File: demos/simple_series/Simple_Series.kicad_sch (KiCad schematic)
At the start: 3 parts, among them SW1 SPST

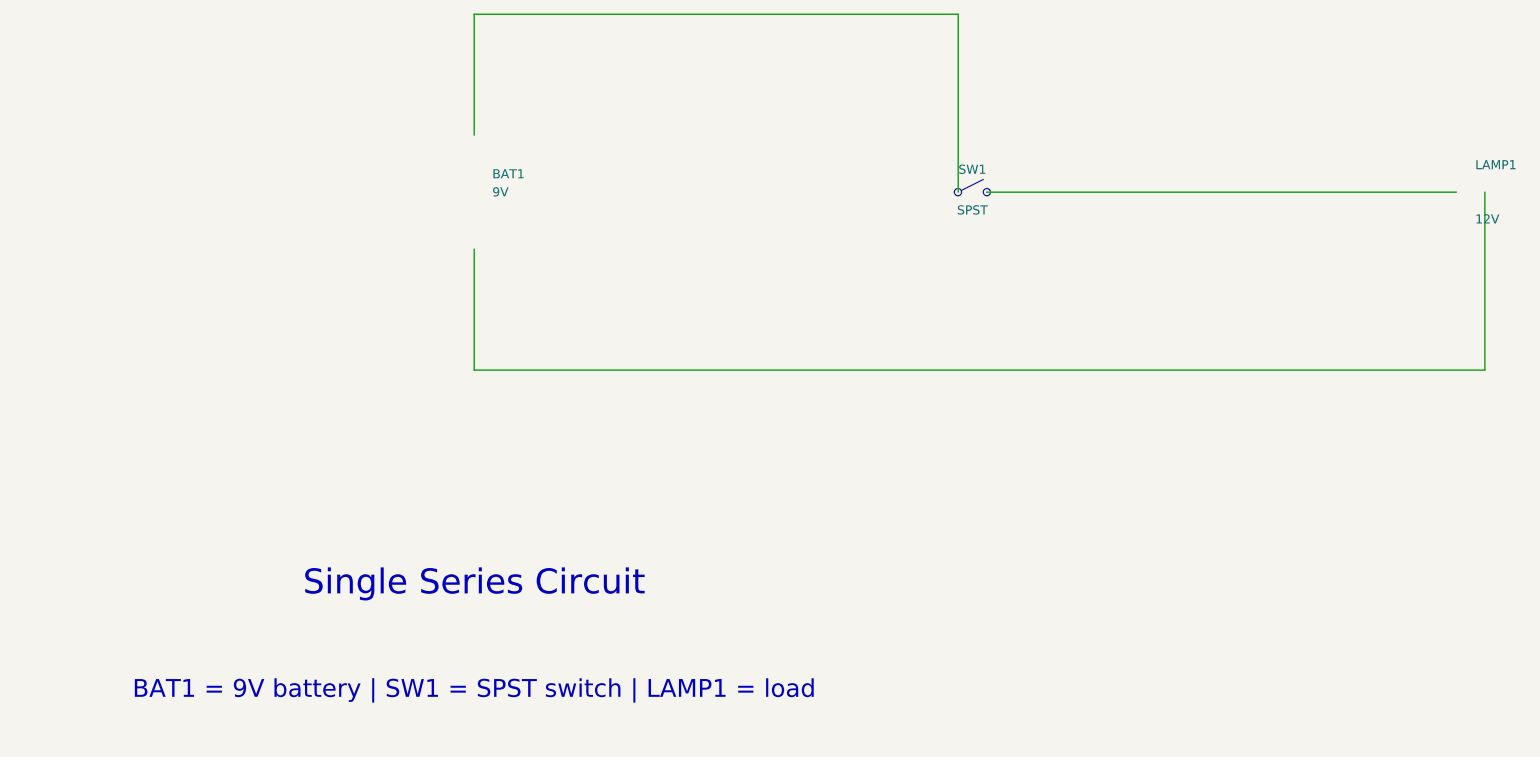
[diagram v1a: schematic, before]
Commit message: feat: pin-aware schematic drawing (connect wires to exact pins)
- kicad_mcp/symbols.py: parse .kicad_sym pin definitions + rotation
  transform (0/90/180/270, matches SCH_SYMBOL transform)
- kicad_sch_add_symbol now returns each pin's absolute coordinate (incl.
  rotation); new kicad_sch_get_symbol_pins and kicad_sch_connect tools
  (connect by pin name, auto-routed Z-shape with optional via point)
- fix float truncation bug: int(x*MM) lost 1 IU (e.g. 134.9199 vs 1349200)
  so wires never joined pins (netlist showed all unconnected); use round()

Verified: redrew single-series circuit with LAMP1 rotated 90; wire endpoints
exactly on pins (134.9200 etc); kicad-cli netlist now shows all 6 pins in a
single connected net.
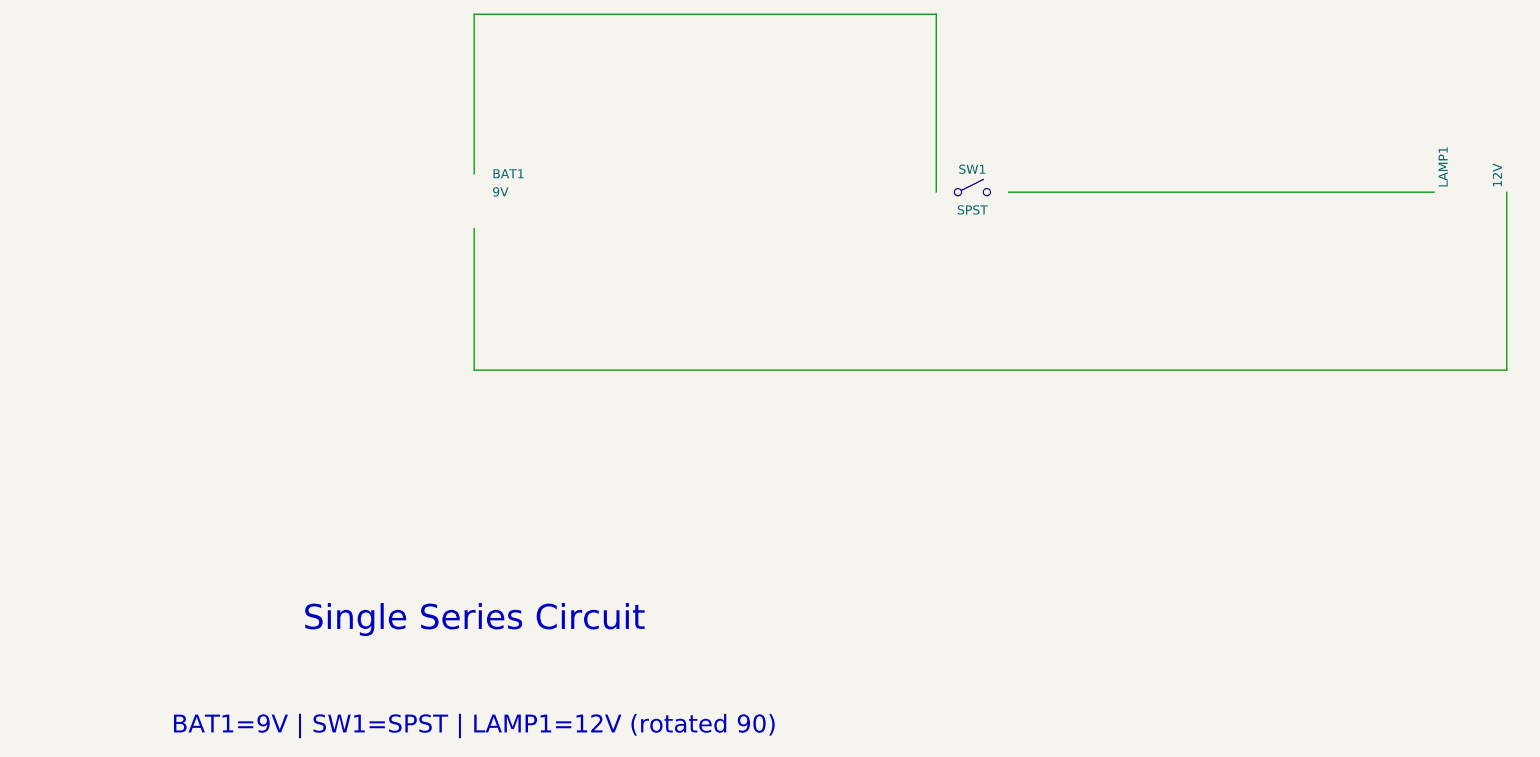
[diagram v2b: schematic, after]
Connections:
- net at SW1.2 (B): now also LAMP1.2 (+)
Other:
- note added: "BAT1=9V | SW1=SPST | LAMP1=12V (rotated 90)"
- note removed: "BAT1 = 9V battery | SW1 = SPST switch | LAMP1 = load"
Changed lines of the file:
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@@
 	(text "Single Series Circuit"
 		(exclude_from_sim no)
-		(at 70 135 0)
+		(at 70 140 0)
 		(effects
 			(font
@@
 		)
 	)
-	(text "BAT1 = 9V battery | SW1 = SPST switch | LAMP1 = load"
-		(exclude_from_sim no)
-		(at 70 150 0)
+	(text "BAT1=9V | SW1=SPST | LAMP1=12V (rotated 90)"
+		(exclude_from_sim no)
+		(at 70 155 0)
 		(effects
 			(font
@@
 	(wire
 		(pts
-			(xy 212 80) (xy 212 105)
-		)
-		(stroke
-			(width 0)
-			(type default)
-		)
-	)
-	(wire
-		(pts
-			(xy 142 80) (xy 208 80)
-		)
-		(stroke
-			(width 0)
-			(type default)
-		)
-	)
-	(wire
-		(pts
-			(xy 70 72) (xy 70 55)
-		)
-		(stroke
-			(width 0)
-			(type default)
-		)
-	)
-	(wire
-		(pts
-			(xy 70 105) (xy 70 88)
-		)
-		(stroke
-			(width 0)
-			(type default)
-		)
-	)
-	(wire
-		(pts
-			(xy 70 55) (xy 138 55)
-		)
-		(stroke
-			(width 0)
-			(type default)
-		)
-	)
-	(wire
-		(pts
-			(xy 138 55) (xy 138 80)
-		)
-		(stroke
-			(width 0)
-			(type default)
-		)
-	)
-	(wire
-		(pts
-			(xy 212 105) (xy 70 105)
-		)
-		(stroke
-			(width 0)
-			(type default)
+			(xy 215.08 80) (xy 215.08 105)
+		)
+		(stroke
+			(width 0)
+			(type default)
+		)
+	)
+	(wire
+		(pts
+			(xy 215.08 105) (xy 70 105)
+		)
+		(stroke
+			(width 0)
+			(type default)
+		)
+	)
+	(wire
+		(pts
+			(xy 70 77.46) (xy 70 55)
+		)
+		(stroke
+			(width 0)
+			(type default)
+		)
+	)
+	(wire
+		(pts
+			(xy 145.08 80) (xy 204.92 80)
+		)
+		(stroke
+			(width 0)
+			(type default)
+		)
+	)
+	(wire
+		(pts
+			(xy 70 105) (xy 70 85.08)
+		)
+		(stroke
+			(width 0)
+			(type default)
+		)
+	)
+	(wire
+		(pts
+			(xy 134.92 55) (xy 134.92 80)
+		)
+		(stroke
+			(width 0)
+			(type default)
+		)
+	)
+	(wire
+		(pts
+			(xy 70 55) (xy 134.92 55)
+		)
+		(stroke
+			(width 0)
+			(type default)
+		)
+	)
+	(symbol
+		(lib_id "Switch:SW_SPST")
+		(at 140 80 0)
+		(unit 1)
+		(body_style 0)
+		(exclude_from_sim no)
+		(in_bom yes)
+		(on_board yes)
+		(in_pos_files yes)
+		(dnp no)
+		(property "Reference" "SW1"
+			(at 140 76.825 0)
+			(show_name no)
+			(do_not_autoplace no)
+			(effects
+				(font
+					(size 1.27 1.27)
+				)
+			)
+		)
+		(property "Value" "SPST"
+			(at 140 82.54 0)
+			(show_name no)
+			(do_not_autoplace no)
+			(effects
+				(font
+					(size 1.27 1.27)
+				)
+			)
+		)
+		(property "Footprint" ""
+			(at 140 80 0)
+			(hide yes)
+			(show_name no)
+			(do_not_autoplace no)
+			(effects
+				(font
+					(size 1.27 1.27)
+				)
+			)
+		)
+		(property "Datasheet" ""
+			(at 140 80 0)
+			(hide yes)
+			(show_name no)
+			(do_not_autoplace no)
+			(effects
+				(font
+					(size 1.27 1.27)
+				)
+			)
+		)
+		(property "Description" "Single Pole Single Throw (SPST) switch"
+			(at 140 80 0)
+			(hide yes)
+			(show_name no)
+			(do_not_autoplace no)
+			(effects
+				(font
+					(size 1.27 1.27)
+				)
+			)
+		)
+		(pin "2"
+		)
+		(pin "1"
+		)
+		(instances
+			(project "Simple_Series"
+				(path "/89df9635-6746-4aa7-a923-2c4181dcf2e4"
+					(reference "SW1")
+					(unit 1)
+				)
+			)
+		)
+	)
+	(symbol
+		(lib_id "Device:Lamp")
+		(at 210 80 90)
+		(unit 1)
+		(body_style 0)
+		(exclude_from_sim no)
+		(in_bom yes)
+		(on_board yes)
+		(in_pos_files yes)
+		(dnp no)
+		(property "Reference" "LAMP1"
+			(at 206.19 79.365 0)
+			(show_name no)
+			(do_not_autoplace no)
+			(effects
+				(font
+					(size 1.27 1.27)
+				)
+				(justify left)
+			)
+		)
+		(property "Value" "12V"
+			(at 213.81 79.365 0)
+			(show_name no)
+			(do_not_autoplace no)
+			(effects
+				(font
+					(size 1.27 1.27)
+				)
+				(justify left)
+			)
+		)
+		(property "Footprint" ""
+			(at 207.46 80 90)
+			(hide yes)
+			(show_name no)
+			(do_not_autoplace no)
+			(effects
+				(font
+					(size 1.27 1.27)
+				)
+			)
+		)
+		(property "Datasheet" ""
+			(at 207.46 80 90)
+			(hide yes)
+			(show_name no)
+			(do_not_autoplace no)
+			(effects
+				(font
+					(size 1.27 1.27)
+				)
+			)
+		)
+		(property "Description" "Lamp"
+			(at 210 80 0)
+			(hide yes)
+			(show_name no)
+			(do_not_autoplace no)
+			(effects
+				(font
+					(size 1.27 1.27)
+				)
+			)
+		)
+		(pin "2"
+		)
+		(pin "1"
+		)
+		(instances
+			(project "Simple_Series"
+				(path "/89df9635-6746-4aa7-a923-2c4181dcf2e4"
+					(reference "LAMP1")
+					(unit 1)
+				)
+			)
 		)
 	)
@@
 		(instances
 			(project "Simple_Series"
-				(path "/fe51f7a9-8c15-422c-9e72-244da0bfb221"
+				(path "/89df9635-6746-4aa7-a923-2c4181dcf2e4"
 					(reference "BAT1")
 					(unit 1)
 				)
-			)
-		)
-	)
-	(symbol
-		(lib_id "Switch:SW_SPST")
-		(at 140 80 0)
-		(unit 1)
-		(body_style 0)
-		(exclude_from_sim no)
-		(in_bom yes)
-		(on_board yes)
-		(in_pos_files yes)
-		(dnp no)
-		(property "Reference" "SW1"
-			(at 140 76.825 0)
-			(show_name no)
-			(do_not_autoplace no)
-			(effects
-				(font
-					(size 1.27 1.27)
-				)
-			)
-		)
-		(property "Value" "SPST"
-			(at 140 82.54 0)
-			(show_name no)
-			(do_not_autoplace no)
-			(effects
-				(font
-					(size 1.27 1.27)
-				)
-			)
-		)
-		(property "Footprint" ""
-			(at 140 80 0)
-			(hide yes)
-			(show_name no)
-			(do_not_autoplace no)
-			(effects
-				(font
-					(size 1.27 1.27)
-				)
-			)
-		)
-		(property "Datasheet" ""
-			(at 140 80 0)
-			(hide yes)
-			(show_name no)
-			(do_not_autoplace no)
-			(effects
-				(font
-					(size 1.27 1.27)
-				)
-			)
-		)
-		(property "Description" "Single Pole Single Throw (SPST) switch"
-			(at 140 80 0)
-			(hide yes)
-			(show_name no)
-			(do_not_autoplace no)
-			(effects
-				(font
-					(size 1.27 1.27)
-				)
-			)
-		)
-		(pin "2"
-		)
-		(pin "1"
-		)
-		(instances
-			(project "Simple_Series"
-				(path "/fe51f7a9-8c15-422c-9e72-244da0bfb221"
-					(reference "SW1")
-					(unit 1)
-				)
-			)
-		)
-	)
-	(symbol
-		(lib_id "Device:Lamp")
-		(at 210 80 0)
-		(unit 1)
-		(body_style 0)
-		(exclude_from_sim no)
-		(in_bom yes)
-		(on_board yes)
-		(in_pos_files yes)
-		(dnp no)
-		(property "Reference" "LAMP1"
-			(at 210.635 76.19 0)
-			(show_name no)
-			(do_not_autoplace no)
-			(effects
-				(font
-					(size 1.27 1.27)
-				)
-				(justify left)
-			)
-		)
-		(property "Value" "12V"
-			(at 210.635 83.81 0)
-			(show_name no)
-			(do_not_autoplace no)
-			(effects
-				(font
-					(size 1.27 1.27)
-				)
-				(justify left)
-			)
-		)
-		(property "Footprint" ""
-			(at 210 77.46 90)
-			(hide yes)
-			(show_name no)
-			(do_not_autoplace no)
-			(effects
-				(font
-					(size 1.27 1.27)
-				)
-			)
-		)
-		(property "Datasheet" ""
-			(at 210 77.46 90)
-			(hide yes)
-			(show_name no)
-			(do_not_autoplace no)
-			(effects
-				(font
-					(size 1.27 1.27)
-				)
-			)
-		)
-		(property "Description" "Lamp"
-			(at 210 80 0)
-			(hide yes)
-			(show_name no)
-			(do_not_autoplace no)
-			(effects
-				(font
-					(size 1.27 1.27)
-				)
-			)
-		)
-		(pin "1"
-		)
-		(pin "2"
-		)
-		(instances
-			(project "Simple_Series"
-				(path "/fe51f7a9-8c15-422c-9e72-244da0bfb221"
-					(reference "LAMP1")
-					(unit 1)
-				)

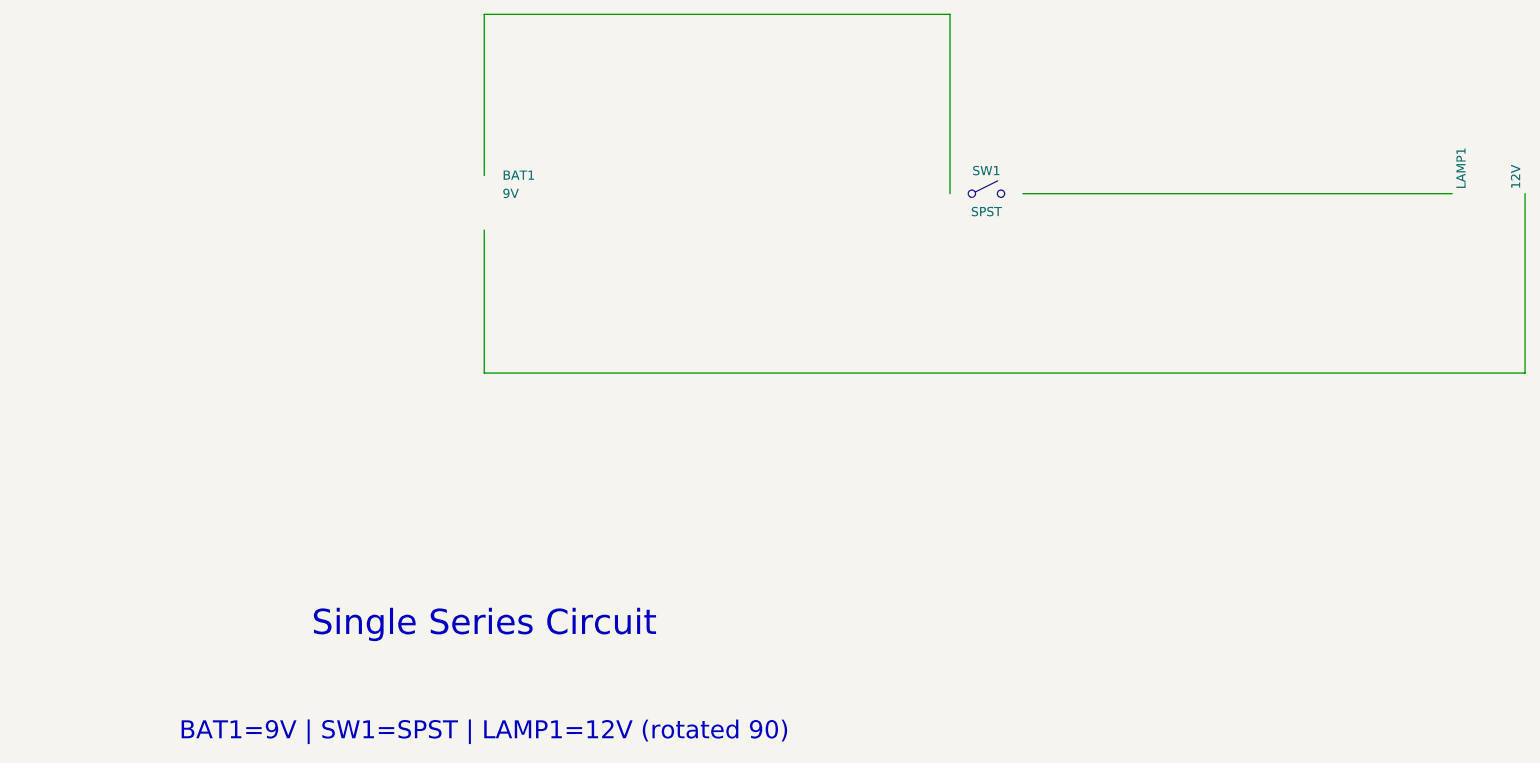
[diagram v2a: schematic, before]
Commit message: feat: KiCad ERC check + exact pin positions (Symbol.pins)
- new kicad_sch_erc MCP tool: runs kicad-cli sch erc and reports
  violations (error/warning); empty report = circuit is truly correct
- Symbol.pins patch: SCH_SYMBOL::Serialize now includes each pin's
  absolute position as computed by KiCad (differs from recomputing from
  the library file by 1 IU or even swapped signs); kicad_sch_connect uses
  these exact positions so wires land precisely on pins
- GetOpenDocuments now fills project.path so clients can resolve the
  full .kicad_sch path (needed by ERC)
- add_symbol snap_to_grid (1.27mm) keeps pins on the ERC connection grid
- kicad_sch_get_symbol_pins reads KiCad pin positions

Verified: single-series circuit (battery+switch+lamp, all horizontal)
passes kicad-cli sch erc with ZERO violations. Key: components on 1.27mm
grid, KiCad pin positions, avoid colinear overlapping wires (rotate
vertical components so pins face left/right).
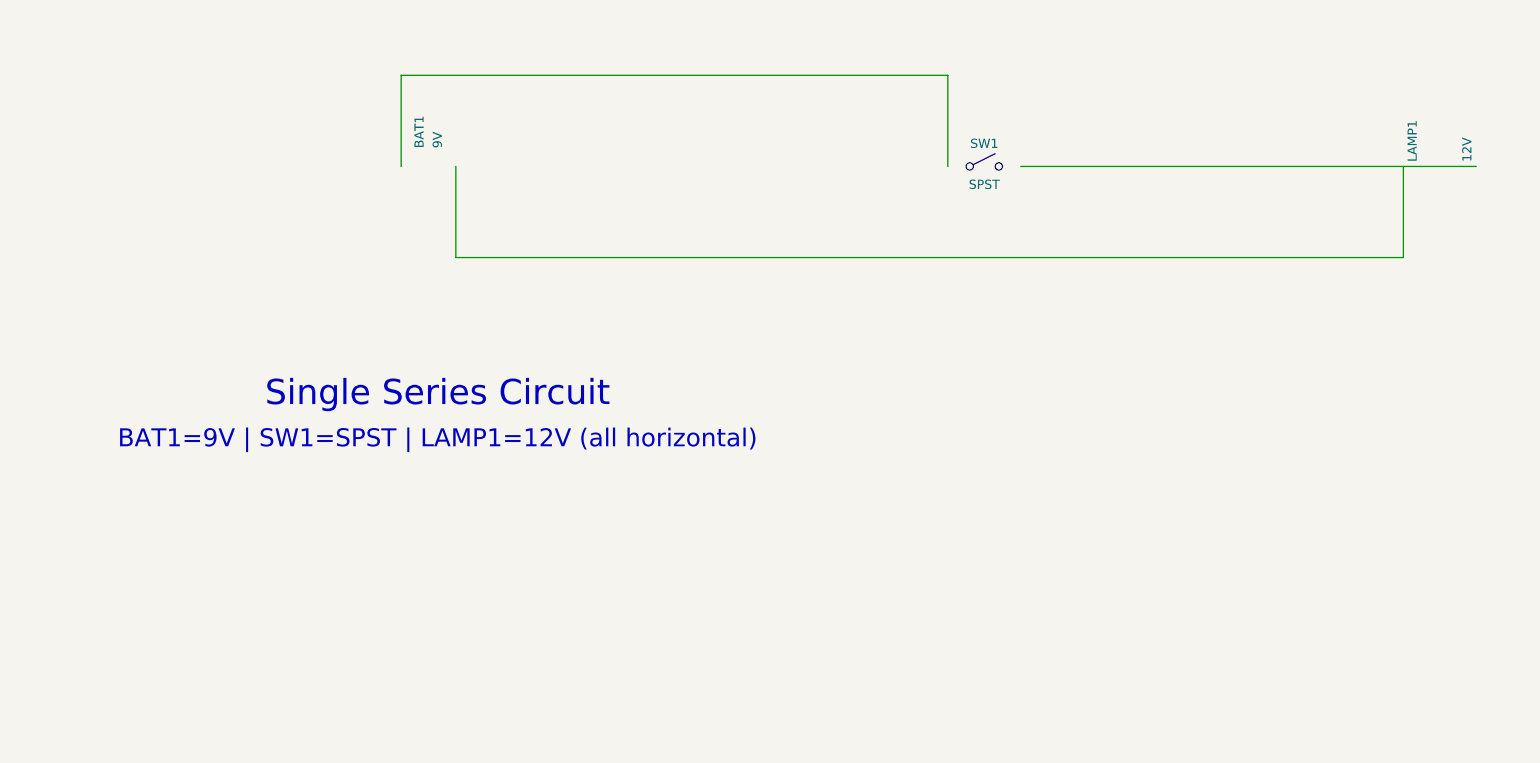
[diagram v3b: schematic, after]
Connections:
- net at SW1.1 (A): now also BAT1.1 (+)
- net at SW1.2 (B): now also LAMP1.1 (-); no longer LAMP1.2 (+)
- net at BAT1.2 (-): now also LAMP1.2 (+)
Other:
- note added: "BAT1=9V | SW1=SPST | LAMP1=12V (all horizontal)"
- note removed: "BAT1=9V | SW1=SPST | LAMP1=12V (rotated 90)"
